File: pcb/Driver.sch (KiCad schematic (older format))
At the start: 25 parts, among them P1 CONN_2, P2 CONN_2, Q1 IRF540N, Q2 IRF540N, T1 ETD29, U1 ArdinoMinPro, U2 MCP14E3

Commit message: Rev 1 working code, schematic updated, pcb todo
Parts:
- removed FerriteBead3: INDUCTOR, Resistors_ThroughHole:Resistor_Horizontal_RM7mm, symbol INDUCTOR
- added C? (x2): 100nF, Capacitors_SMD:C_0805_HandSoldering, symbol C
- added D?: 1N5819, Resistors_ThroughHole:Resistor_Horizontal_RM7mm, symbol DIODE
- added R? (x3): 120R, Resistors_SMD:R_0805_HandSoldering, symbol R
- added U?: LM7808ACT, TO-220, symbol LM7808ACT
- C1: renamed from 100nF1; value C -> 100nF
- C2: renamed from 4700uF1; value CAPAPOL -> 4700uF 50V
- C3: renamed from 10uF1; value CAPAPOL -> 330uF 50v; footprint Capacitors_SMD:C_1210_HandSoldering -> Capacitors_ThroughHole:C_Radial_D8_L11.5_P3.5
- C4: renamed from 1uF1; value CAPAPOL -> 100uF
- C5: renamed from 470nF1; value C -> 470nF
- C6: renamed from 100nF2; value C -> 1uF
- C7: renamed from 1uF2; value CAPAPOL -> 1uF
- C8: renamed from 100nF3; value C -> 100nF
- Q1, Q2: value IRF540N -> RPF60N06
- R1: renamed from 100K1; value R -> 100K
- R2: renamed from 22K1; value R -> 22K
- U2: value MCP14E3 -> MCP14E4
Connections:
- net 12v: now also C?.1, D?.2 (K), U?.1 (IN); no longer C4.1, C6.1, U1.24 (RAW)
- net ENPWM: now also R?.1; no longer U1.14 (MOSI)
- net GND: now also C?.2, C?.2, U?.2 (GND)
- net PWMA: now also R?.1; no longer U1.13 (D10)
- net PWMB: now also R?.2; no longer U1.12 (D9)
- net at F1.1, P2.2 (PM): now also D?.1 (A)
- new net: R?.1, U1.12 (D9)
- new net: R?.2, U1.13 (D10)
- new net: R?.2, U1.14 (MOSI)
- new net 8v: C4.1, C6.1, C?.1, U1.24 (RAW), U?.3 (OUT)
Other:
- note added: "Peak Drive current IRF540N = Q/dT = 95/39 = 2.4A \nRFP50N06 = 125/55 = 2.27A\nDriver Power\nIRF540N = 1400E-12*12*12*250E3 = 50mW\nRFP50N06 = 2200E-12*12*12*250E3 = 80mW\n\nMCP14E3 can deliver 4.5A at 18V and will drive at about 15ns for 1400pF@12V gate.\nIt will disipate 1.1W\n\nhttp://ww1.microchip.com/downloads/en/Appnotes/00799b.pdf\n\nClampin diodes on the mosfet gates mitigate latch up due 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"
- note removed: "Peak Drive current IRF540N = Q/dT = 95/39 = 2.4A \nRFP50N06 = 125/55 = 2.27A\nDriver Power\nIRF540N = 1400E-12*12*12*250E3 = 50mW\nRFP50N06 = 2200E-12*12*12*250E3 = 80mW\n\nMCP14E3 can deliver 4.5A at 18V and will drive at about 15ns for 1400pF@12V gate.\nIt will disipate 1.1W\n\nhttp://ww1.microchip.com/downloads/en/Appnotes/00799b.pdf\n\n\n\n"
- moved on the sheet: C1, C4, C6, R1, R2, U1

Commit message: Added loadswitch to avoid inrush
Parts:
- removed D1: 1N5819, Resistors_ThroughHole:Resistor_Horizontal_RM7mm, symbol DIODE
- added C10: 10uF, Capacitors_SMD:C_0805_HandSoldering, symbol C
- added C11: 100nF, Capacitors_SMD:C_0805_HandSoldering, symbol C
- added C9: 10nF, Capacitors_SMD:C_0805_HandSoldering, symbol C
- added D7, D8: 1N5819, symbol DIODESCH
- added D9: 1N5819, Resistors_ThroughHole:Resistor_Horizontal_RM7mm, symbol DIODESCH
- added L1: 330uH 5A TBC, symbol INDUCTOR
- added Q?: IRF540N, TO220, symbol IRF540N
- added R3: 120R, Resistors_SMD:R_0805_HandSoldering, symbol R
- added R5: 22R, Resistors_SMD:R_0805_HandSoldering, symbol R
- added R6, R7: 100K, Resistors_SMD:R_0805_HandSoldering, symbol R
- added R8: 22K, Resistors_SMD:R_0805_HandSoldering, symbol R
- D1: renamed from D?; symbol DIODE -> DIODESCH
- D2, D3, D4, D5, D6: symbol DIODE -> DIODESCH
- U3: renamed from U?; footprint TO-220 -> Power_Integrations:TO-220
- gave numbers to parts that had none: 5
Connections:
- net 12v: now also D1.1 (A), F1.1, P2.2 (PM); no longer C12.1, D1.2 (K), U3.1 (IN)
- net 12vPower: now also L1.2, R7.1
- net 8v: now also C12.1; no longer C4.1
- net GND: now also C11.2, D9.1 (A), R8.2
- net at U1.11 (D8): now also R3.1
- net at R9.2: now also U1.15 (MISO); no longer U1.14 (MOSI)
- net ADC2: now reaches U1.18 (A1)
- net ADC2: now also C11.1, R7.2, R8.1
- net at F1.2: now also Q?.2 (D)
- new net: C4.1, R5.1, U3.1 (IN)
- new net: D1.2 (K), R5.2
- new net: C10.1, D8.1 (A), D9.2 (K), L1.1, Q?.3 (S), R6.2
- new net: C10.2, D7.2 (K), Q?.1 (G), R6.1
- new net: C9.1, D7.1 (A), D8.2 (K)
- new net PWRENABLE: C9.2, R3.2, U1.14 (MOSI)
- no-connect marks 28 -> 25
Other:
- note removed: "Protect 12v input from freqhencies generated by driver"
- moved on the sheet: C12, C2, C3, C4, C5, D1, R9, U3

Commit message: Working version with soft start, some frequency adjustments to come
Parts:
- removed C12: 100nF, Capacitors_SMD:C_0805_HandSoldering, symbol C
- removed R3: 120R, Resistors_SMD:R_0805_HandSoldering, symbol R
- C10: footprint Capacitors_SMD:C_0805_HandSoldering -> Capacitors_ThroughHole:C_Radial_D8_L11.5_P3.5
- C2: footprint Capacitors_ThroughHole:C_Radial_D22_L41_P10 -> Capacitors_ThroughHole:C_Radial_D18_L36_P7.5
- C4: footprint Capacitors_SMD:C_1210_HandSoldering -> Capacitors_ThroughHole:C_Radial_D8_L11.5_P3.5
- D7, D8: footprint (none) -> Resistors_ThroughHole:Resistor_Horizontal_RM7mm
- L1: footprint (none) -> Divers:Choke14x32
- P1: footprint Connect:AK300-2 -> Connect:AK300-3; symbol CONN_2 -> CONN_3
- Q3: renamed from Q?; value IRF540N -> IRL540; footprint TO220 -> TO_SOT_Packages_SMD:TO-263-3Lead
- U3: footprint Power_Integrations:TO-220 -> TO_SOT_Packages_SMD:TO-263-3Lead
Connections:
- net GND: now also P1.3 (P3)
- net at D5.1 (A), D6.2 (K), U2.5 (OUT_B): now also Q2.1 (G); no longer Q1.1 (G)
- net at D2.1 (A), D3.2 (K), U2.7 (OUT_A): now also Q1.1 (G); no longer Q2.1 (G)
- no-connect marks 25 -> 26
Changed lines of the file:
@@
 F 0 "C2" H 5100 6700 40  0000 L CNN
 F 1 "4700uF 50V" H 5100 6500 40  0000 L CNN
-F 2 "Capacitors_ThroughHole:C_Radial_D22_L41_P10" H 5150 6450 30  0001 C CNN
+F 2 "Capacitors_ThroughHole:C_Radial_D18_L36_P7.5" H 5150 6450 30  0001 C CNN
 F 3 "" H 5050 6600 300 0000 C CNN
 	1    5050 6600
@@
 Ultrasound Driver
 $Comp
-L CONN_2 P1
+L CONN_3 P1
 U 1 1 6082AEB0
 P 10600 2500
 F 0 "P1" V 10550 2500 40  0000 C CNN
 F 1 "CONN_2" V 10650 2500 40  0000 C CNN
-F 2 "Connect:AK300-2" H 10600 2500 60  0001 C CNN
+F 2 "Connect:AK300-3" H 10600 2500 60  0001 C CNN
 F 3 "" H 10600 2500 60  0001 C CNN
 	1    10600 2500
@@
 F 0 "C4" H 2400 5500 40  0000 L CNN
 F 1 "100uF" H 2400 5300 40  0000 L CNN
-F 2 "Capacitors_SMD:C_1210_HandSoldering" H 2450 5250 30  0001 C CNN
+F 2 "Capacitors_ThroughHole:C_Radial_D8_L11.5_P3.5" H 2450 5250 30  0001 C CNN
 F 3 "" H 2350 5400 300 0000 C CNN
 	1    2350 5400
@@
 	1    0    0    -1
 $EndComp
-$Comp
-L C C12
-U 1 1 608EE669
-P 3550 5450
-F 0 "C12" H 3550 5550 40  0000 L CNN
-F 1 "100nF" H 3556 5365 40  0000 L CNN
-F 2 "Capacitors_SMD:C_0805_HandSoldering" H 3588 5300 30  0001 C CNN
-F 3 "" H 3550 5450 60  0000 C CNN
-	1    3550 5450
-	1    0    0    -1
-$EndComp
 Text GLabel 4350 1200 2    60   Input ~ 0
 8v
@@
 F 0 "U3" H 2700 5350 40  0000 C CNN
 F 1 "LM7808ACT" H 2900 5350 40  0000 L CNN
-F 2 "Power_Integrations:TO-220" H 2900 5250 30  0000 C CIN
+F 2 "TO_SOT_Packages_SMD:TO-263-3Lead" H 2900 5250 30  0000 C CIN
 F 3 "" H 2900 5150 60  0000 C CNN
 	1    2900 5150
@@
 F 0 "C10" H 3000 7000 40  0000 L CNN
 F 1 "10uF" H 3006 6815 40  0000 L CNN
-F 2 "Capacitors_SMD:C_0805_HandSoldering" H 3038 6750 30  0001 C CNN
+F 2 "Capacitors_ThroughHole:C_Radial_D8_L11.5_P3.5" H 3038 6750 30  0001 C CNN
 F 3 "" H 3000 6900 60  0000 C CNN
 	1    3000 6900
@@
 F 0 "L1" V 4150 6200 40  0000 C CNN
 F 1 "330uH 5A TBC" V 4300 6200 40  0000 C CNN
-F 2 "" H 4200 6200 60  0001 C CNN
+F 2 "Divers:Choke14x32" H 4200 6200 60  0001 C CNN
 F 3 "" H 4200 6200 60  0000 C CNN
 	1    4200 6200
@@
 Connection ~ 6450 1900
 Wire Wire Line
-	7050 2350 7450 2350
-Wire Wire Line
-	7450 2350 7450 2300
-Wire Wire Line
-	7450 2300 8050 2300
-Wire Wire Line
-	6900 2500 7450 2500
-Wire Wire Line
-	7450 2500 7450 3050
-Wire Wire Line
 	7450 3050 8050 3050
 Wire Wire Line
@@
 	5000 3150 5100 3150
 Connection ~ 5000 3100
-Wire Wire Line
-	6950 2200 6950 3000
-Connection ~ 6950 2500
-Wire Wire Line
-	7250 2200 7250 3000
-Connection ~ 7250 2350
 Wire Wire Line
 	6950 1800 6950 1650
@@
 	3400 1900 3150 1900
 Wire Wire Line
-	10250 2600 10100 2600
-Wire Wire Line
-	10100 2600 10100 2700
+	10100 2500 10100 2700
 Wire Wire Line
 	10100 2700 10050 2700
@@
 	5900 3450 5900 3750
 Wire Wire Line
-	6900 2500 6900 2350
-Wire Wire Line
-	6900 2350 6650 2350
-Wire Wire Line
-	7050 2350 7050 2450
-Wire Wire Line
-	7050 2450 6800 2450
-Wire Wire Line
-	6800 2450 6800 2500
-Wire Wire Line
-	6800 2500 6650 2500
+	6650 2350 7450 2350
 Connection ~ 4100 1200
 Connection ~ 1100 6200
@@
 	3300 5100 3850 5100
 Wire Wire Line
-	3550 5250 3550 5100
-Connection ~ 3550 5100
-Wire Wire Line
 	2900 5400 2900 5900
 Wire Wire Line
-	2350 5750 3550 5750
+	2350 5750 2900 5750
 Wire Wire Line
 	2350 5750 2350 5600
-Wire Wire Line
-	3550 5750 3550 5650
 Connection ~ 2900 5750
 Wire Wire Line
@@
 Wire Wire Line
 	3400 1800 3150 1800
-Text GLabel 950  2200 0    60   Output ~ 0
-PWRENABLE
-$Comp
-L R R3
-U 1 1 6090F189
-P 1200 2200
-F 0 "R3" V 1280 2200 40  0000 C CNN
-F 1 "120R" V 1207 2201 40  0000 C CNN
-F 2 "Resistors_SMD:R_0805_HandSoldering" V 1130 2200 30  0001 C CNN
-F 3 "" H 1200 2200 30  0000 C CNN
-	1    1200 2200
-	0    1    1    0
-$EndComp
-Wire Wire Line
-	1450 2200 1650 2200
 Wire Wire Line
 	3400 2100 3150 2100
@@
 F 0 "D8" H 3300 7200 40  0000 C CNN
 F 1 "1N5819" H 3300 7000 40  0000 C CNN
-F 2 "" H 3300 7100 60  0001 C CNN
+F 2 "Resistors_ThroughHole:Resistor_Horizontal_RM7mm" H 3300 7100 60  0001 C CNN
 F 3 "" H 3300 7100 60  0000 C CNN
 	1    3300 7100
@@
 F 0 "D7" H 2750 7200 40  0000 C CNN
 F 1 "1N5819" H 2750 7000 40  0000 C CNN
-F 2 "" H 2750 7100 60  0001 C CNN
+F 2 "Resistors_ThroughHole:Resistor_Horizontal_RM7mm" H 2750 7100 60  0001 C CNN
 F 3 "" H 2750 7100 60  0000 C CNN
 	1    2750 7100
@@
 	3800 6900 3800 7250
 $Comp
-L IRF540N Q?
+L IRF540N Q3
 U 1 1 609311A2
 P 2650 6300
-F 0 "Q?" H 2650 6152 40  0000 R CNN
-F 1 "IRF540N" H 2650 6449 40  0000 R CNN
-F 2 "TO220" H 2471 6401 29  0000 C CNN
+F 0 "Q3" H 2650 6152 40  0000 R CNN
+F 1 "IRL540" H 2650 6449 40  0000 R CNN
+F 2 "TO_SOT_Packages_SMD:TO-263-3Lead" H 2471 6401 29  0000 C CNN
 F 3 "" H 2650 6300 60  0000 C CNN
 	1    2650 6300
 	0    -1   -1   0
 $EndComp
+NoConn ~ 1650 2200
+Wire Wire Line
+	7250 2200 7250 3000
+Wire Wire Line
+	6650 2500 7450 2500
+Connection ~ 7250 2500
+Wire Wire Line
+	7450 2500 7450 3050
+Wire Wire Line
+	6950 2200 6950 3000
+Connection ~ 6950 2350
+Wire Wire Line
+	7450 2350 7450 2300
+Wire Wire Line
+	7450 2300 8050 2300
+Wire Wire Line
+	10100 2500 10250 2500
+$Comp
+L GND #PWR013
+U 1 1 60941517
+P 10200 2800
+F 0 "#PWR013" H 10200 2800 30  0001 C CNN
+F 1 "GND" H 10200 2730 30  0001 C CNN
+F 2 "" H 10200 2800 60  0001 C CNN
+F 3 "" H 10200 2800 60  0001 C CNN
+	1    10200 2800
+	1    0    0    -1
+$EndComp
+Wire Wire Line
+	10250 2600 10200 2600
+Wire Wire Line
+	10200 2600 10200 2800
 $EndSCHEMATC

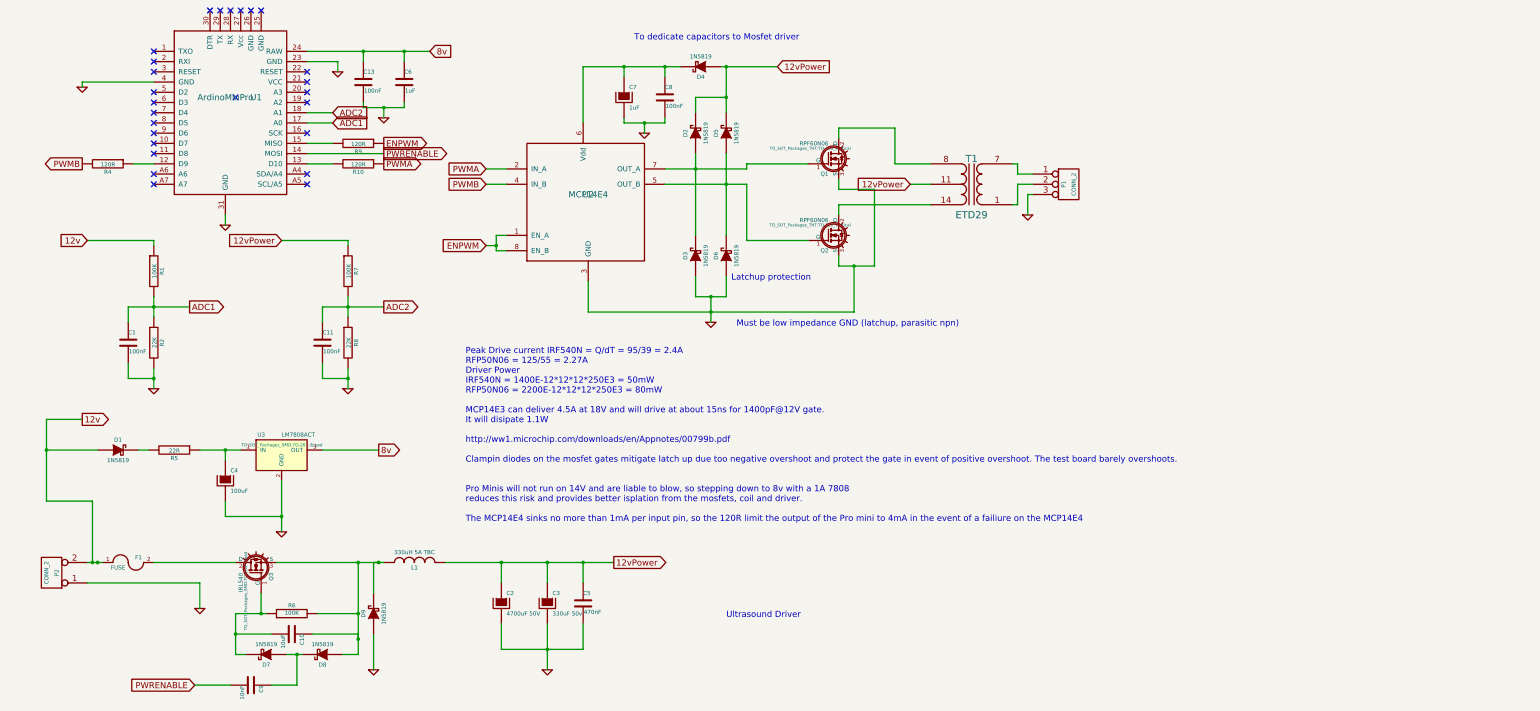
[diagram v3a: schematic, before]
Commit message: v2 board complete with temperature sensor on power components
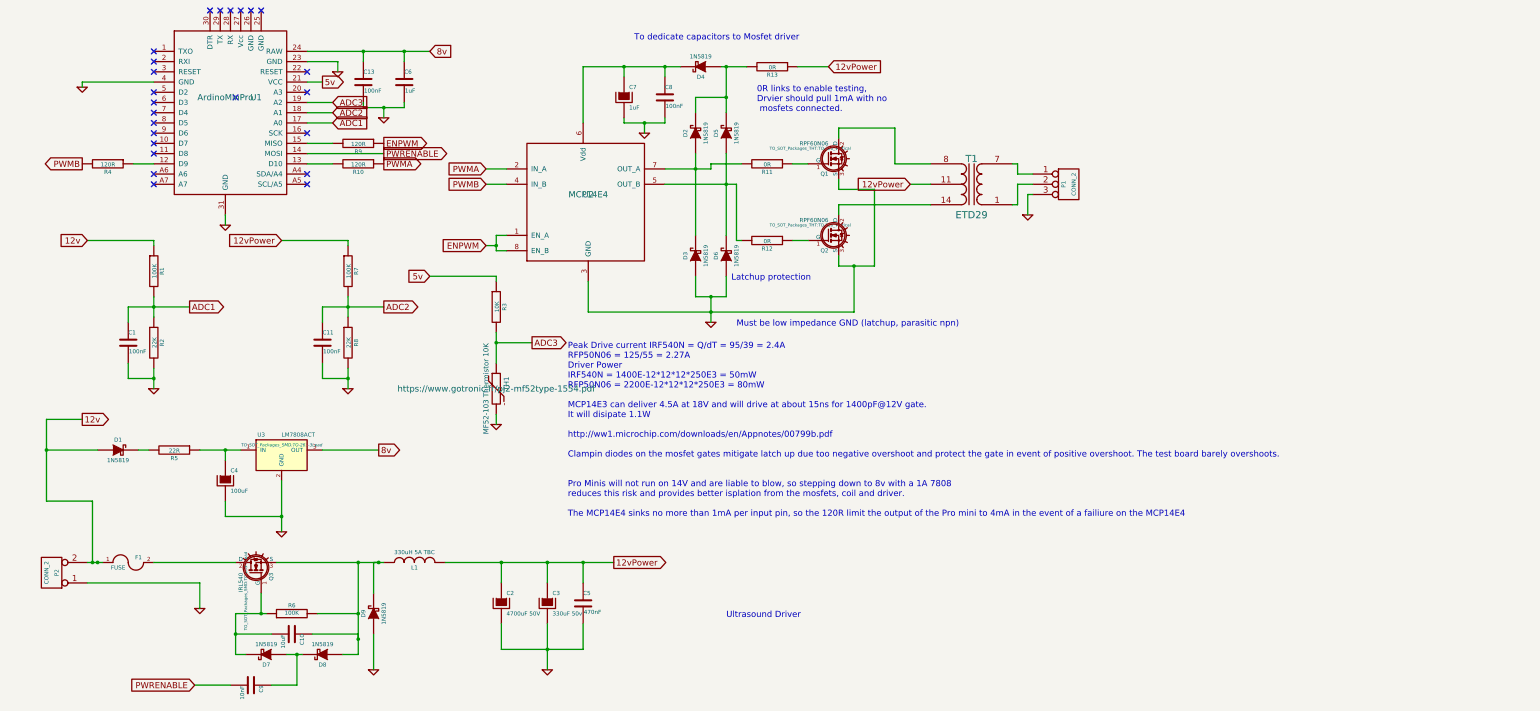
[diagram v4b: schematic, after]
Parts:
- added R11, R12, R13: 0R, Resistors_SMD:R_0805_HandSoldering, symbol R
- added R3: 10K, Resistors_SMD:R_0805_HandSoldering, symbol R
- added TH1: MF52-103 Thermistor 10K, Pin_Headers:Pin_Header_Straight_1x02_Pitch2.54mm, symbol THERMISTOR
- C6: footprint Capacitors_SMD:C_0805_HandSoldering -> Capacitors_SMD:C_1210_HandSoldering
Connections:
- net 12vPower: now also R13.1; no longer D2.2 (K), D4.1 (A), D5.2 (K)
- net GND: now also TH1.2
- net ADC3: now reaches U1.19 (A2)
- net ADC3: now also R3.2, TH1.1
- net 5v: now reaches U1.21 (VCC)
- net 5v: now also R3.1
- net at D5.1 (A), D6.2 (K), U2.5 (OUT_B): now also R12.2; no longer Q2.1 (G)
- net at D2.1 (A), D3.2 (K), U2.7 (OUT_A): now also R11.2; no longer Q1.1 (G)
- new net: Q1.1 (G), R11.1
- new net: Q2.1 (G), R12.1
- new net: D2.2 (K), D4.1 (A), D5.2 (K), R13.2
- no-connect marks 26 -> 24
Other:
- note added: "0R links to enable testing, \nDrvier should pull 1mA with no\n mosfets connected."
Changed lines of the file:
@@
 $EndDescr
-$Comp
-L ArdinoMinPro U1
-U 1 1 6081B080
-P 2350 1650
-F 0 "U1" H 2650 1650 60  0000 C CNN
-F 1 "ArdinoMinPro" H 2350 1650 60  0000 C CNN
-F 2 "Divers:ArduinoProMini" H 2650 1650 60  0001 C CNN
-F 3 "" H 2650 1650 60  0001 C CNN
-	1    2350 1650
-	1    0    0    -1
-$EndComp
 $Comp
 L MCP14E3 U2
@@
 	1    0    0    -1
 $EndComp
-Text GLabel 7750 1350 2    60   Input ~ 0
+Text GLabel 8250 1350 2    60   Input ~ 0
 12vPower
 $Comp
@@
 	-1   0    0    1
 $EndComp
-Text Notes 4700 6100 0    60   ~ 0
+Text Notes 5700 6050 0    60   ~ 0
 Peak Drive current IRF540N = Q/dT = 95/39 = 2.4A \nRFP50N06 = 125/55 = 2.27A\nDriver Power\nIRF540N = 1400E-12*12*12*250E3 = 50mW\nRFP50N06 = 2200E-12*12*12*250E3 = 80mW\n\nMCP14E3 can deliver 4.5A at 18V and will drive at about 15ns for 1400pF@12V gate.\nIt will disipate 1.1W\n\nhttp://ww1.microchip.com/downloads/en/Appnotes/00799b.pdf\n\nClampin diodes on the mosfet gates mitigate latch up due too negative overshoot and protect the gate in event of positive overshoot. The test board barely overshoots.\n\n\nPro Minis will not run on 14V and are liable to blow, so stepping down to 8v with a 1A 7808\nreduces this risk and provides better isplation from the mosfets, coil and driver.\n\nThe MCP14E4 sinks no more than 1mA per input pin, so the 120R limit the output of the Pro mini to 4mA in the event of a failiure on the MCP14E4\n\n\n\n
 Text GLabel 6150 6200 2    60   Output ~ 0
@@
 F 0 "C6" H 4100 1600 40  0000 L CNN
 F 1 "1uF" H 4106 1415 40  0000 L CNN
-F 2 "Capacitors_SMD:C_0805_HandSoldering" H 4138 1350 30  0001 C CNN
+F 2 "Capacitors_SMD:C_1210_HandSoldering" H 4138 1350 30  0001 C CNN
 F 3 "" H 4100 1500 60  0000 C CNN
 	1    4100 1500
@@
 ADC1
 NoConn ~ 3150 1400
-NoConn ~ 3150 1500
 NoConn ~ 3150 1600
-NoConn ~ 3150 1700
 NoConn ~ 3150 2000
 NoConn ~ 3150 2400
@@
 Connection ~ 6450 1900
 Wire Wire Line
-	7450 3050 8050 3050
-Wire Wire Line
 	8350 2450 8350 2550
 Wire Wire Line
@@
 Connection ~ 7100 3600
 Wire Wire Line
-	7200 1350 7750 1350
+	7200 1350 7450 1350
 Connection ~ 7250 1350
 Connection ~ 7250 1650
@@
 Wire Wire Line
 	5900 3450 5900 3750
-Wire Wire Line
-	6650 2350 7450 2350
 Connection ~ 4100 1200
 Connection ~ 1100 6200
@@
 Wire Wire Line
 	7250 2200 7250 3000
-Wire Wire Line
-	6650 2500 7450 2500
 Connection ~ 7250 2500
-Wire Wire Line
-	7450 2500 7450 3050
 Wire Wire Line
 	6950 2200 6950 3000
 Connection ~ 6950 2350
-Wire Wire Line
-	7450 2350 7450 2300
-Wire Wire Line
-	7450 2300 8050 2300
 Wire Wire Line
 	10100 2500 10250 2500
@@
 Wire Wire Line
 	10200 2600 10200 2800
+$Comp
+L R R11
+U 1 1 609E3987
+P 7650 2300
+F 0 "R11" V 7730 2300 40  0000 C CNN
+F 1 "0R" V 7657 2301 40  0000 C CNN
+F 2 "Resistors_SMD:R_0805_HandSoldering" V 7580 2300 30  0001 C CNN
+F 3 "" H 7650 2300 30  0000 C CNN
+	1    7650 2300
+	0    1    1    0
+$EndComp
+$Comp
+L R R12
+U 1 1 609E3A7D
+P 7650 3050
+F 0 "R12" V 7730 3050 40  0000 C CNN
+F 1 "0R" V 7657 3051 40  0000 C CNN
+F 2 "Resistors_SMD:R_0805_HandSoldering" V 7580 3050 30  0001 C CNN
+F 3 "" H 7650 3050 30  0000 C CNN
+	1    7650 3050
+	0    1    1    0
+$EndComp
+$Comp
+L R R13
+U 1 1 609E3D60
+P 7700 1350
+F 0 "R13" V 7780 1350 40  0000 C CNN
+F 1 "0R" V 7707 1351 40  0000 C CNN
+F 2 "Resistors_SMD:R_0805_HandSoldering" V 7630 1350 30  0001 C CNN
+F 3 "" H 7700 1350 30  0000 C CNN
+	1    7700 1350
+	0    1    1    0
+$EndComp
+Wire Wire Line
+	7950 1350 8250 1350
+Wire Wire Line
+	6650 2350 7100 2350
+Wire Wire Line
+	7100 2350 7100 2300
+Wire Wire Line
+	7100 2300 7400 2300
+Wire Wire Line
+	7900 2300 8050 2300
+Wire Wire Line
+	7900 3050 8050 3050
+Wire Wire Line
+	7400 3050 7350 3050
+Wire Wire Line
+	7350 3050 7350 2500
+Wire Wire Line
+	7350 2500 6650 2500
+Text Notes 7550 1800 0    60   ~ 0
+0R links to enable testing, \nDrvier should pull 1mA with no\n mosfets connected.
+$Comp
+L R R3
+U 1 1 609E4DDE
+P 5000 3700
+F 0 "R3" V 5080 3700 40  0000 C CNN
+F 1 "10K" V 5007 3701 40  0000 C CNN
+F 2 "Resistors_SMD:R_0805_HandSoldering" V 4930 3700 30  0001 C CNN
+F 3 "" H 5000 3700 30  0000 C CNN
+	1    5000 3700
+	1    0    0    -1
+$EndComp
+$Comp
+L GND #PWR014
+U 1 1 609E4DEA
+P 5000 4850
+F 0 "#PWR014" H 5000 4850 30  0001 C CNN
+F 1 "GND" H 5000 4780 30  0001 C CNN
+F 2 "" H 5000 4850 60  0001 C CNN
+F 3 "" H 5000 4850 60  0001 C CNN
+	1    5000 4850
+	1    0    0    -1
+$EndComp
+Text GLabel 4350 3400 0    60   Input ~ 0
+5v
+Text GLabel 5350 4050 2    60   Output ~ 0
+ADC3
+Wire Wire Line
+	4350 3400 5000 3400
+Wire Wire Line
+	5000 3400 5000 3450
+Wire Wire Line
+	5000 3950 5000 4250
+Wire Wire Line
+	5000 4050 5350 4050
+Connection ~ 5000 4050
+$Comp
+L THERMISTOR TH1
+U 1 1 609E5290
+P 5000 4500
+F 0 "TH1" V 5100 4550 50  0000 C CNN
+F 1 "MF52-103 Thermistor 10K" V 4900 4500 50  0000 C CNN
+F 2 "Pin_Headers:Pin_Header_Straight_1x02_Pitch2.54mm" H 5000 4500 60  0001 C CNN
+F 3 "https://www.gotronic.fr/pj2-mf52type-1554.pdf" H 5000 4500 60  0000 C CNN
+	1    5000 4500
+	1    0    0    -1
+$EndComp
+Wire Wire Line
+	5000 4750 5000 4850
+Text GLabel 3400 1700 2    60   Input ~ 0
+ADC3
+$Comp
+L ArdinoMinPro U1
+U 1 1 6081B080
+P 2350 1650
+F 0 "U1" H 2650 1650 60  0000 C CNN
+F 1 "ArdinoMinPro" H 2350 1650 60  0000 C CNN
+F 2 "Divers:ArduinoProMini" H 2650 1650 60  0001 C CNN
+F 3 "" H 2650 1650 60  0001 C CNN
+	1    2350 1650
+	1    0    0    -1
+$EndComp
+Wire Wire Line
+	3400 1700 3150 1700
+Text GLabel 3300 1500 2    60   Output ~ 0
+5v
+Wire Wire Line
+	3150 1500 3300 1500
 $EndSCHEMATC
